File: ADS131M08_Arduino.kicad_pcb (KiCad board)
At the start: 2 copper layers, 68.6 x 53.3 mm, 35 parts, among them J1 Power, J2 Digital/PWM, J3 Analog, J4 Digital/PWM, J5 Conn_02x12_Odd_Even, U1 ADS131M08IPB, X1 SiT8008

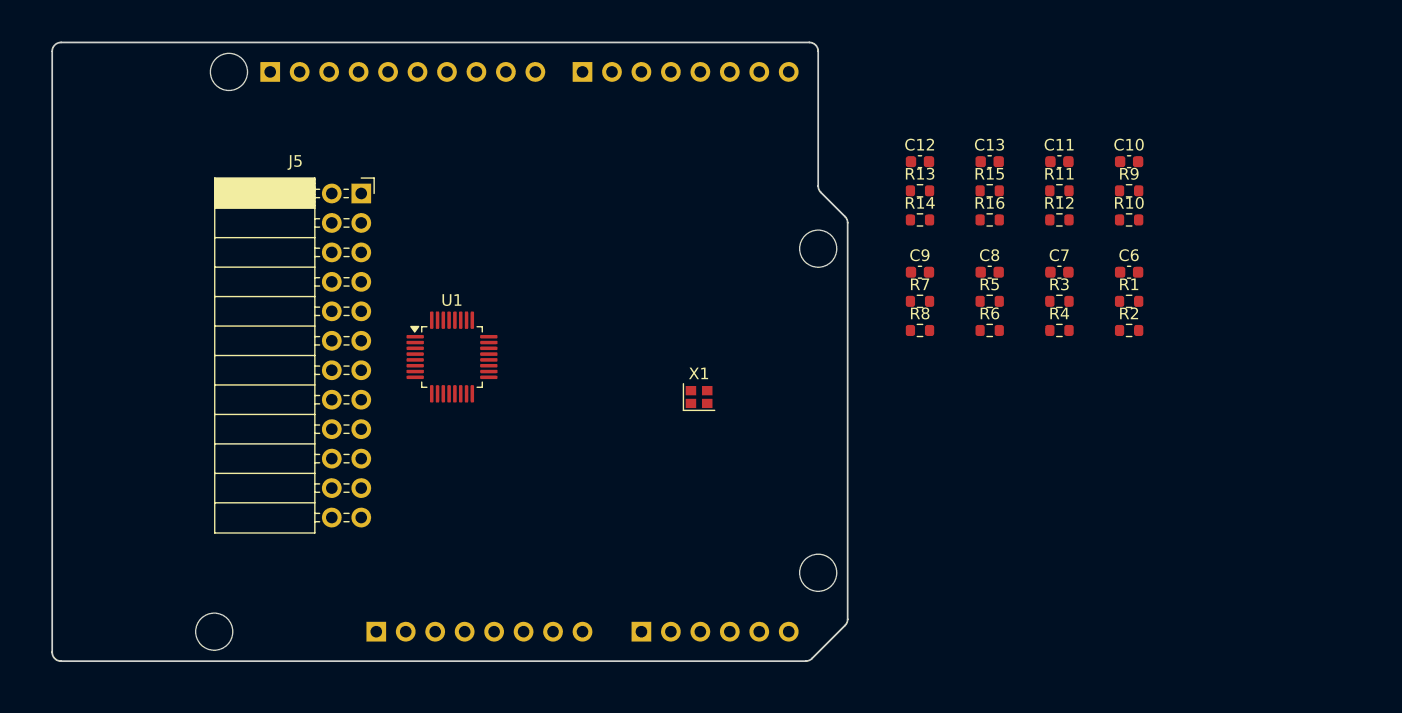
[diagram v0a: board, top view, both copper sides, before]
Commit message: Updated to use resistor arrays
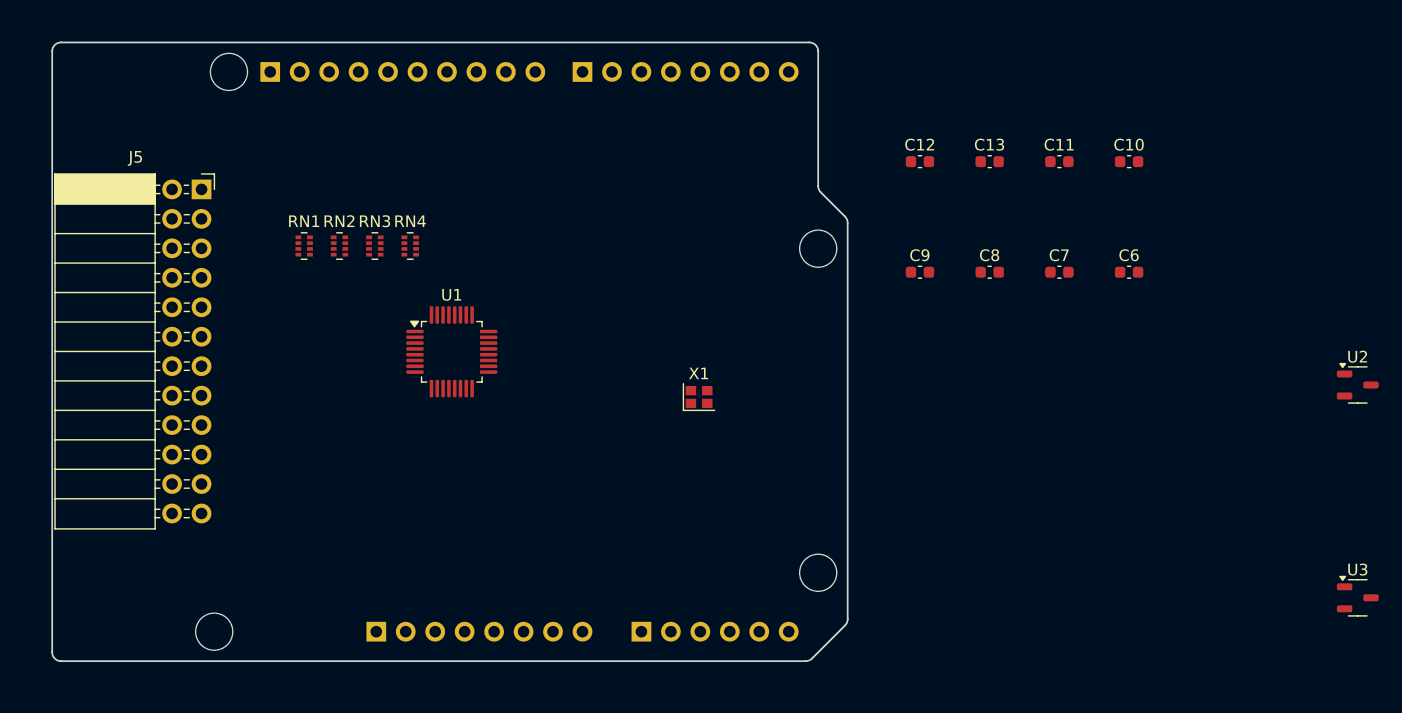
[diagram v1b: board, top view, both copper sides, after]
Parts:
- removed R1, R10, R11, R12, R13, R14, R15, R16, R2, R3, R4, R5, R6, R7, R8, R9: 10kR, Resistor_SMD:R_0603_1608Metric
- added RN1: 10kR, Resistor_SMD:R_Array_Concave_4x0402, F.Cu at (121.7, 64.2)
- added RN2: 10kR, Resistor_SMD:R_Array_Concave_4x0402, F.Cu at (124.8, 64.2)
- added RN3: 10kR, Resistor_SMD:R_Array_Concave_4x0402, F.Cu at (127.8, 64.2)
- added RN4: 10kR, Resistor_SMD:R_Array_Concave_4x0402, F.Cu at (130.9, 64.2)
- added U2: XC6206PxxxMR, Package_TO_SOT_SMD:SOT-23-3, F.Cu at (212.6, 76.2)
- added U3: XC6206PxxxMR, Package_TO_SOT_SMD:SOT-23-3, F.Cu at (212.6, 94.5)
- moved J5 13.8 mm to (112.9, 59.3)
- moved U1 0.45 mm to (134.4, 73.3)
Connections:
- net /Antialiasing/ADC+ renamed /AIN0P
- net /Antialiasing/ADC- renamed /AIN0N
- net /Antialiasing1/ADC+ renamed /AIN1P
- net /Antialiasing1/ADC- renamed /AIN1N
- net /Antialiasing2/ADC+ renamed /AIN2P
- net /Antialiasing2/ADC- renamed /AIN2N
- net /Antialiasing3/ADC+ renamed /AIN3P
- net /Antialiasing3/ADC- renamed /AIN3N
- net /Antialiasing4/ADC+ renamed /AIN4P
- net /Antialiasing4/ADC- renamed /AIN4N
- net /Antialiasing5/ADC+ renamed /AIN5P
- net /Antialiasing5/ADC- renamed /AIN5N
- net /Antialiasing6/ADC+ renamed /AIN6P
- net /Antialiasing6/ADC- renamed /AIN6N
- net /Antialiasing7/ADC+ renamed /AIN7P
- net /Antialiasing7/ADC- renamed /AIN7N
- J5 pad 1: unconnected-(J5-Pin_1-Pad1) -> +5V
- J5 pad 21: unconnected-(J5-Pin_21-Pad21) -> GND
- J5 pad 22: unconnected-(J5-Pin_22-Pad22) -> GND
- J5 pad 3: unconnected-(J5-Pin_3-Pad3) -> GND
- J5 pad 4: unconnected-(J5-Pin_4-Pad4) -> GND
- U1 pad 15: Net-(U1-AVDD) -> +3.3VADC
- U1 pad 16: /*9 -> /8
- U1 pad 17: /*10 -> /*9
- U1 pad 18: /8 -> /*10
- U1 pad 26: Net-(U1-DVDD) -> +3.3V

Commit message: Commit nov 9 2024
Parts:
- added C1: 1uF, Capacitor_SMD:C_0402_1005Metric, F.Cu at (136.2, 68.6)
- added C14: 1uF, Capacitor_SMD:C_0402_1005Metric, F.Cu at (136.7, 85.8)
- added C15: 1uF, Capacitor_SMD:C_0402_1005Metric, F.Cu at (135.8, 65.0)
- added C16: 1uF, Capacitor_SMD:C_0402_1005Metric, F.Cu at (141.0, 65.0)
- added C17: 1uF, Capacitor_SMD:C_0402_1005Metric, F.Cu at (136.7, 80.5)
- added C2: 1uF, Capacitor_SMD:C_0402_1005Metric, F.Cu at (136.7, 78.1)
- added C3: 100nF, Capacitor_SMD:C_0402_1005Metric, F.Cu at (135.2, 78.6)
- added C4: 220nF, Capacitor_SMD:C_0402_1005Metric, F.Cu at (138.3, 70.6)
- added C5: 100nF, Capacitor_SMD:C_0402_1005Metric, F.Cu at (143.0, 71.5)
- C10, C11, C12, C13, C6, C7, C8, C9: footprint Capacitor_SMD:C_0603_1608Metric -> Capacitor_SMD:C_0402_1005Metric
- moved C10 77.3 mm to (117.6, 74.8), turned to -90 degrees
- moved U3 76.7 mm to (136.7, 83.1), turned to -90 degrees
- moved C6 75.3 mm to (117.6, 64.8), turned to -90 degrees
- moved U2 75.0 mm to (138.4, 65.0)
- moved C11 72.0 mm to (117.6, 76.8), turned to 90 degrees
- moved C7 69.2 mm to (117.6, 66.7), turned to 90 degrees
- moved C13 68.0 mm to (117.6, 81.9), turned to 90 degrees
- moved C8 63.3 mm to (117.6, 69.8), turned to -90 degrees
- moved C12 61.7 mm to (117.6, 79.9), turned to -90 degrees
- moved C9 57.5 mm to (117.6, 71.8), turned to 90 degrees
- moved RN4 22.4 mm to (116.0, 80.9), turned to 180 degrees
- moved X1 15.8 mm to (141.0, 71.5), turned to 180 degrees
- moved RN2 14.6 mm to (116.0, 75.8), turned to 180 degrees
- moved RN3 11.9 mm to (116.0, 65.7), turned to 180 degrees
- moved RN1 8.70 mm to (116.0, 70.8), turned to 180 degrees
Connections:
- J3 pad 5: /SDA/A4 -> unconnected-(J3-Pin_5-Pad5)
- J3 pad 6: /SCL/A5 -> unconnected-(J3-Pin_6-Pad6)
- J5 pad 1: +5V -> /SDA/A4
- J5 pad 2: unconnected-(J5-Pin_2-Pad2) -> /SCL/A5
- J5 pad 23: unconnected-(J5-Pin_23-Pad23) -> /A0
- J5 pad 24: unconnected-(J5-Pin_24-Pad24) -> +5V
- RN1 pad 1: /IN3- -> /AIN3P
- RN1 pad 2: /IN3+ -> /AIN3N
- RN1 pad 3: /IN2- -> /AIN2N
- RN1 pad 4: /IN2+ -> /AIN2P
- RN1 pad 5: /AIN2P -> /IN2+
- RN1 pad 6: /AIN2N -> /IN2-
- RN1 pad 7: /AIN3P -> /IN3+
- RN1 pad 8: /AIN3N -> /IN3-
- RN2 pad 1: /IN5- -> /AIN5P
- RN2 pad 2: /IN5+ -> /AIN5N
- RN2 pad 3: /IN4- -> /AIN4N
- RN2 pad 4: /IN4+ -> /AIN4P
- RN2 pad 5: /AIN4P -> /IN4+
- RN2 pad 6: /AIN4N -> /IN4-
- RN2 pad 7: /AIN5P -> /IN5+
- RN2 pad 8: /AIN5N -> /IN5-
- RN3 pad 1: /IN1- -> /AIN1P
- RN3 pad 2: /IN1+ -> /AIN1N
- RN3 pad 3: /IN0- -> /AIN0N
- RN3 pad 4: /IN0+ -> /AIN0P
- RN3 pad 5: /AIN0P -> /IN0+
- RN3 pad 6: /AIN0N -> /IN0-
- RN3 pad 7: /AIN1P -> /IN1+
- RN3 pad 8: /AIN1N -> /IN1-
- RN4 pad 1: /IN7- -> /AIN7P
- RN4 pad 2: /IN7+ -> /AIN7N
- RN4 pad 3: /IN6- -> /AIN6N
- RN4 pad 4: /IN6+ -> /AIN6P
- RN4 pad 5: /AIN6P -> /IN6+
- RN4 pad 6: /AIN6N -> /IN6-
- RN4 pad 7: /AIN7P -> /IN7+
- RN4 pad 8: /AIN7N -> /IN7-
- U1 pad 19: /13 -> /*11
- U1 pad 21: /*11 -> /13
- X1 pad 4: Net-(X1-VDD) -> +3.3V
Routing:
- net +5V: track 0.00 -> 85.8 mm, vias 0 -> 2
- net /A0: track 0.00 -> 43.3 mm
- net /12: track 0.00 -> 42.4 mm
- net /13: track 0.00 -> 42.3 mm
- net /*11: track 0.00 -> 41.8 mm
- net /8: track 0.00 -> 41.2 mm
- net /*10: track 0.00 -> 40.7 mm
- net /*9: track 0.00 -> 39.7 mm
- net /AIN7P: track 0.00 -> 23.3 mm
- net /AIN0P: track 0.00 -> 23.2 mm
- net /AIN0N: track 0.00 -> 21.6 mm
- net /AIN7N: track 0.00 -> 21.6 mm
- net +3.3V: track 0.00 -> 19.8 mm, vias 0 -> 2
- net /AIN1N: track 0.00 -> 19.7 mm
- net /AIN6N: track 0.00 -> 19.7 mm
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- added copper zone on B.Cu, net GND
- added copper zone on F.Cu, net GND
- added copper zone on In1.Cu, net GND
- added copper zone on In2.Cu, net GND
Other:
- copper layers 2 -> 4
- board text added: "ADS131M08 24-bit 8-channel ΔΣ ADC"
